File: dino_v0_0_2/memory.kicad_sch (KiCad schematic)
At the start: 10 parts, among them U19 74LS245, U21 74LS245, U24 AT28C256, U26 MCM60256AP, U51 7400

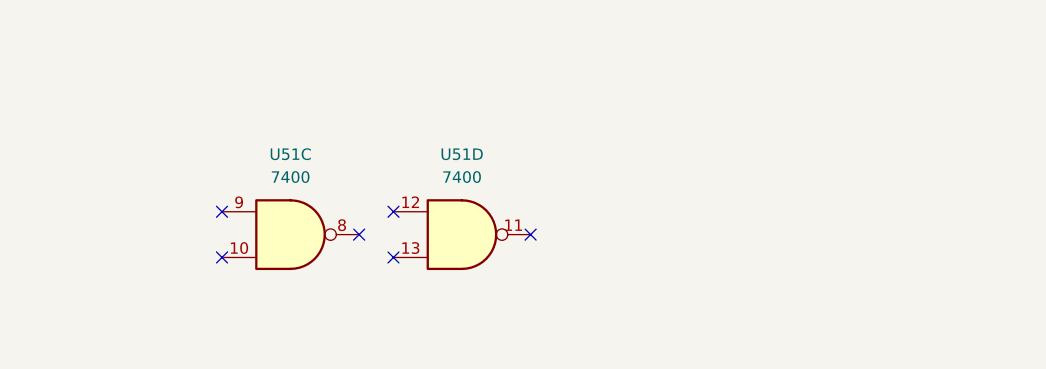
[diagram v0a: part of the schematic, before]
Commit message: feat(dino): generate + stamp per-sheet I/O contracts
Each module's boundary signals (IN/OUT/BIDIR with counterpart sheets)
derived from the kicad-cli netlist and placed as a text block on the
physical sheet, so a bench rig knows exactly what to drive and observe
per board. kicad_contracts.py regenerates both the markdown and the
stamps idempotently; stamping verified electrically neutral.
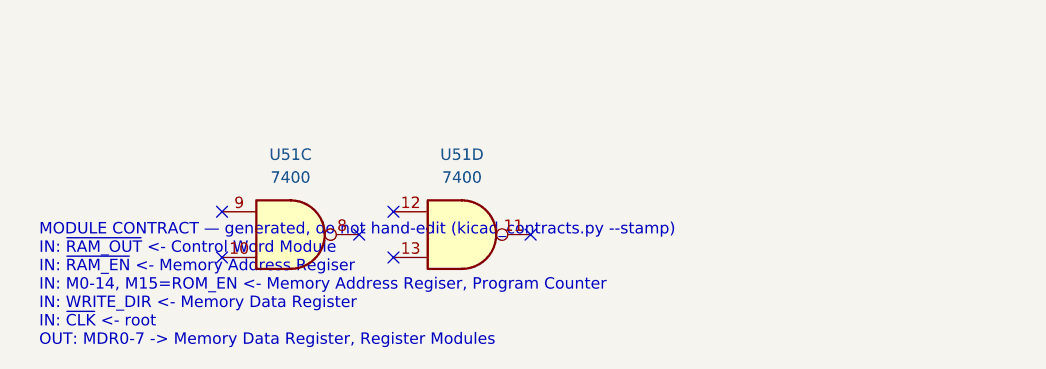
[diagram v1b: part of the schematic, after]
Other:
- note added: "MODULE CONTRACT — generated, do not hand-edit (kicad_contracts.py --stamp) IN: ~{RAM_OUT} <- Control Word Module IN: ~{RAM_EN} <- Memory Address Regiser IN: M0-14, M15=ROM_EN <- Memory Address Regiser, Program Counter IN: WRITE_DIR <- Memory Data Register IN: ~{CLK} <- root OUT: MDR0-7 -> Memory Data Register, Register Modules"
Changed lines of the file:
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@@
+		)
+	)
+	(text "MODULE CONTRACT — generated, do not hand-edit (kicad_contracts.py --stamp)\nIN: ~{RAM_OUT} <- Control Word Module\nIN: ~{RAM_EN} <- Memory Address Regiser\nIN: M0-14, M15=ROM_EN <- Memory Address Regiser, Program Counter\nIN: WRITE_DIR <- Memory Data Register\nIN: ~{CLK} <- root\nOUT: MDR0-7 -> Memory Data Register, Register Modules"
+		(exclude_from_sim no)
+		(at 15.24 209.39 0)
+		(effects
+			(font
+				(size 1.27 1.27)
+			)
+			(justify left bottom)
 		)
 	)

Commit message: fix(dino): three review-found schematic bugs on microcode/memory
- microcode U9/U15: ~WE tied +5V, A12 tied GND (were floating with NC
  flags — in-circuit corruption + image-aliasing hazard on AT28C64B)
- memory: label the U24.~OE/U19.CE net ~{ROM_OUT} — the ROM read path
  had no driver as drawn (caught by new kicad_netlist.py --lint)
- memory: U21 (RAM-side '245) CE now AND(~RAM_OUT, ~WRITE_DIR) via U51
  spare gates — was enabled by ~RAM_EN alone, buffering floating RAM DQ
  onto MDR against register drivers whenever MAR parked on a RAM
  address with no RAM op in flight

Contracts restamped; all verified in kicad_netlist.py + kicad-cli
export; lint clean project-wide.
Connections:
- net ~{RAM_EN}: no longer U21.19 (CE)
- net ~{RAM_OUT}: now also U51.9
- net ~{WRITE_DIR}: now also U51.10
- net ~{RAM_MDR_EN}: now reaches U51.11
- net ~{RAM_MDR_EN}: now also U21.19 (CE)
- net RAM_MDR_DIS: now reaches U51.12
- net RAM_MDR_DIS: now also U51.13, U51.8
- net ~{ROM_OUT}: now reaches U19.19 (CE), U24.22 (~{OE})
- no-connect marks 9 -> 3
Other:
- note added: "MODULE CONTRACT — generated, do not hand-edit (kicad_contracts.py --stamp) IN: ~{RAM_OUT}, ~{ROM_OUT} <- Control Word Module IN: ~{RAM_EN} <- Memory Address Regiser IN: M0-14, M15=ROM_EN <- Memory Address Regiser, Program Counter IN: WRITE_DIR <- Memory Data Register IN: ~{CLK} <- root OUT: MDR0-7 -> Memory Data Register, Register Modules"
- note removed: "MODULE CONTRACT — generated, do not hand-edit (kicad_contracts.py --stamp) IN: ~{RAM_OUT} <- Control Word Module IN: ~{RAM_EN} <- Memory Address Regiser IN: M0-14, M15=ROM_EN <- Memory Address Regiser, Program Counter IN: WRITE_DIR <- Memory Data Register IN: ~{CLK} <- root OUT: MDR0-7 -> Memory Data Register, Register Modules"
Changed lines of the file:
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@@
 	)
 	(no_connect
-		(at 54.61 194.31)
-	)
-	(no_connect
-		(at 35.56 194.31)
-	)
-	(no_connect
-		(at 54.61 199.39)
-	)
-	(no_connect
-		(at 35.56 199.39)
-	)
-	(no_connect
-		(at 50.8 196.85)
-	)
-	(no_connect
 		(at 93.98 27.94)
 	)
@@
 		(at 57.15 115.57)
 	)
-	(no_connect
-		(at 69.85 196.85)
-	)
 	(bus_entry
 		(at 148.59 76.2)
@@
 	(wire
 		(pts
-			(xy 109.22 83.82) (xy 109.22 111.76)
-		)
-		(stroke
-			(width 0)
-			(type default)
-		)
-	)
-	(wire
-		(pts
 			(xy 93.98 66.04) (xy 95.25 66.04)
 		)
@@
 		)
 	)
-	(text "MODULE CONTRACT — generated, do not hand-edit (kicad_contracts.py --stamp)\nIN: ~{RAM_OUT} <- Control Word Module\nIN: ~{RAM_EN} <- Memory Address Regiser\nIN: M0-14, M15=ROM_EN <- Memory Address Regiser, Program Counter\nIN: WRITE_DIR <- Memory Data Register\nIN: ~{CLK} <- root\nOUT: MDR0-7 -> Memory Data Register, Register Modules"
+	(label "~{ROM_OUT}"
+		(at 194.31 83.82 0)
+		(effects
+			(font
+				(size 1.27 1.27)
+			)
+			(justify left bottom)
+		)
+	)
+	(wire
+		(pts
+			(xy 35.56 194.31) (xy 30.48 194.31)
+		)
+		(stroke
+			(width 0)
+			(type default)
+		)
+	)
+	(label "~{RAM_OUT}"
+		(at 30.48 194.31 180)
+		(effects
+			(font
+				(size 1.27 1.27)
+			)
+			(justify right bottom)
+		)
+	)
+	(wire
+		(pts
+			(xy 35.56 199.39) (xy 30.48 199.39)
+		)
+		(stroke
+			(width 0)
+			(type default)
+		)
+	)
+	(label "~{WRITE_DIR}"
+		(at 30.48 199.39 180)
+		(effects
+			(font
+				(size 1.27 1.27)
+			)
+			(justify right bottom)
+		)
+	)
+	(wire
+		(pts
+			(xy 50.8 196.85) (xy 55.88 196.85)
+		)
+		(stroke
+			(width 0)
+			(type default)
+		)
+	)
+	(label "RAM_MDR_DIS"
+		(at 55.88 196.85 0)
+		(effects
+			(font
+				(size 1.27 1.27)
+			)
+			(justify left bottom)
+		)
+	)
+	(wire
+		(pts
+			(xy 54.61 194.31) (xy 49.53 194.31)
+		)
+		(stroke
+			(width 0)
+			(type default)
+		)
+	)
+	(label "RAM_MDR_DIS"
+		(at 49.53 194.31 180)
+		(effects
+			(font
+				(size 1.27 1.27)
+			)
+			(justify right bottom)
+		)
+	)
+	(wire
+		(pts
+			(xy 54.61 199.39) (xy 49.53 199.39)
+		)
+		(stroke
+			(width 0)
+			(type default)
+		)
+	)
+	(label "RAM_MDR_DIS"
+		(at 49.53 199.39 180)
+		(effects
+			(font
+				(size 1.27 1.27)
+			)
+			(justify right bottom)
+		)
+	)
+	(wire
+		(pts
+			(xy 69.85 196.85) (xy 74.93 196.85)
+		)
+		(stroke
+			(width 0)
+			(type default)
+		)
+	)
+	(label "~{RAM_MDR_EN}"
+		(at 74.93 196.85 0)
+		(effects
+			(font
+				(size 1.27 1.27)
+			)
+			(justify left bottom)
+		)
+	)
+	(wire
+		(pts
+			(xy 109.22 83.82) (xy 104.14 83.82)
+		)
+		(stroke
+			(width 0)
+			(type default)
+		)
+	)
+	(label "~{RAM_MDR_EN}"
+		(at 104.14 83.82 180)
+		(effects
+			(font
+				(size 1.27 1.27)
+			)
+			(justify right bottom)
+		)
+	)
+	(text "MODULE CONTRACT — generated, do not hand-edit (kicad_contracts.py --stamp)\nIN: ~{RAM_OUT}, ~{ROM_OUT} <- Control Word Module\nIN: ~{RAM_EN} <- Memory Address Regiser\nIN: M0-14, M15=ROM_EN <- Memory Address Regiser, Program Counter\nIN: WRITE_DIR <- Memory Data Register\nIN: ~{CLK} <- root\nOUT: MDR0-7 -> Memory Data Register, Register Modules"
 		(exclude_from_sim no)
 		(at 15.24 209.39 0)
